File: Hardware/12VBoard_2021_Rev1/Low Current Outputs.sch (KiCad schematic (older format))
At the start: 54 parts

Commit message: Changed things
Dans a quitter
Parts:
- removed C?: 1000 uF, symbol Device:CP1
- removed C?: 100uF, symbol Device:C_Small
- removed Conn? (x2): AndersonPP, symbol MRDT_Connectors:AndersonPP
- removed D?: D_Schottky, symbol Device:D_Schottky
- removed D?: LED, symbol Device:LED
- removed L?: 100 uH, Inductor_SMD:L_0603_1608Metric_Pad1.05x0.95mm_HandSolder, symbol Device:L
- removed R?: 25m, symbol Device:R
- removed R?: 1.2k, symbol Device:R
- removed SW?: SW_SPDT, symbol Switch:SW_SPDT
- removed TP? (x2): TestPoint, symbol Connector:TestPoint
- removed U?: LM2576D2TR4, MRDT_Devices:LM2576, symbol 12VBoard_2021_Rev1-rescue:LM2576D2TR4-MRDT_Devices
- removed U?: INA198, Package_TO_SOT_SMD:SOT-23-5, symbol Amplifier_Current:INA198
- added R?: 25m, symbol Device:R
- added TP? (x2): TestPoint, symbol Connector:TestPoint
- added U?: INA198, Package_TO_SOT_SMD:SOT-23-5, symbol Amplifier_Current:INA198
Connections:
- net 5V: now also U?.3 (V+)
- net CurrentSense: now also TP?.1, U?.1
- net ExtraToggle: now also U?.5 (ON/OFF), TP?.1
- net GND: now also U?.2 (GND)
- net PackVoltage: now also R?.2, U?.4 (+); no longer C?.1, C?.1, C?.1, C?.1, U?.1 (VIN), U?.1 (VIN), U?.1 (VIN), U?.1 (VIN)
- net at C?.1, L?.2, U?.4 (FEEDBACK): now also Conn?.2 (V+Log), Conn?.2 (V+Log), R?.1
- new net: C?.1, C?.1, C?.1, C?.1, R?.1, U?.1 (VIN), U?.1 (VIN), U?.1 (VIN), U?.1 (VIN), U?.5 (-)

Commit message: Changed buck names
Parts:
- U? (x4): value LM2576D2TR4 -> LM2576S-12/NOPB
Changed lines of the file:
@@
 AR Path="/5F74F223/5F850762" Ref="U?"  Part="1"
 F 0 "U?" H 3100 1700 50  0000 C CNN
-F 1 "LM2576D2TR4" H 3100 1609 50  0000 C CNN
+F 1 "LM2576S-12/NOPB" H 3100 1609 50  0000 C CNN
 F 2 "MRDT_Devices:LM2576" H 3100 1725 50  0001 C CNN
 F 3 "https://www.mouser.com/datasheet/2/308/LM2576_D-1810688.pdf" H 3100 1725 50  0001 C CNN
@@
 AR Path="/5F74F223/5F853A40" Ref="U?"  Part="1"
 F 0 "U?" H 3125 2975 50  0000 C CNN
-F 1 "LM2576D2TR4" H 3125 2884 50  0000 C CNN
+F 1 "LM2576S-12/NOPB" H 3125 2884 50  0000 C CNN
 F 2 "MRDT_Devices:LM2576" H 3125 3000 50  0001 C CNN
 F 3 "https://www.mouser.com/datasheet/2/308/LM2576_D-1810688.pdf" H 3125 3000 50  0001 C CNN
@@
 AR Path="/5F74F223/5F8580AC" Ref="U?"  Part="1"
 F 0 "U?" H 3150 4225 50  0000 C CNN
-F 1 "LM2576D2TR4" H 3150 4134 50  0000 C CNN
+F 1 "LM2576S-12/NOPB" H 3150 4134 50  0000 C CNN
 F 2 "MRDT_Devices:LM2576" H 3150 4250 50  0001 C CNN
 F 3 "https://www.mouser.com/datasheet/2/308/LM2576_D-1810688.pdf" H 3150 4250 50  0001 C CNN
@@
 AR Path="/5F74F223/5F86A2E0" Ref="U?"  Part="1"
 F 0 "U?" H 3250 7000 50  0000 C CNN
-F 1 "LM2576D2TR4" H 3250 6909 50  0000 C CNN
+F 1 "LM2576S-12/NOPB" H 3250 6909 50  0000 C CNN
 F 2 "MRDT_Devices:LM2576" H 3250 7025 50  0001 C CNN
 F 3 "https://www.mouser.com/datasheet/2/308/LM2576_D-1810688.pdf" H 3250 7025 50  0001 C CNN

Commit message: fixed some stuffs
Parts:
- C10, C3, C4, C5, C6, C7, C8, C9: renamed from C?; footprint (none) -> Capacitor_SMD:C_0603_1608Metric_Pad1.05x0.95mm_HandSolder
- Conn1: renamed from Conn?; footprint (none) -> MRDT_Connectors:Anderson_2_Horizontal_Stacked
- D10, D11, D4, D5, D6, D7, D8, D9: renamed from D?; footprint (none) -> Diode_SMD:D_0603_1608Metric_Pad1.05x0.95mm_HandSolder
- R3: renamed from R?; value 25m -> 500m
- R4, R5, R6, R7: renamed from R?; footprint (none) -> Resistor_SMD:R_0603_1608Metric_Pad1.05x0.95mm_HandSolder
- TP1, TP2, TP3, TP4: renamed from TP?; footprint (none) -> TestPoint:TestPoint_Pad_2.5x2.5mm
- gave numbers to parts that had none: 14
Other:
- moved on the sheet: C10, C6, Conn6B, Conn7A, Conn7B, Conn8A, D11, D7, L5, R7, TP3, U6

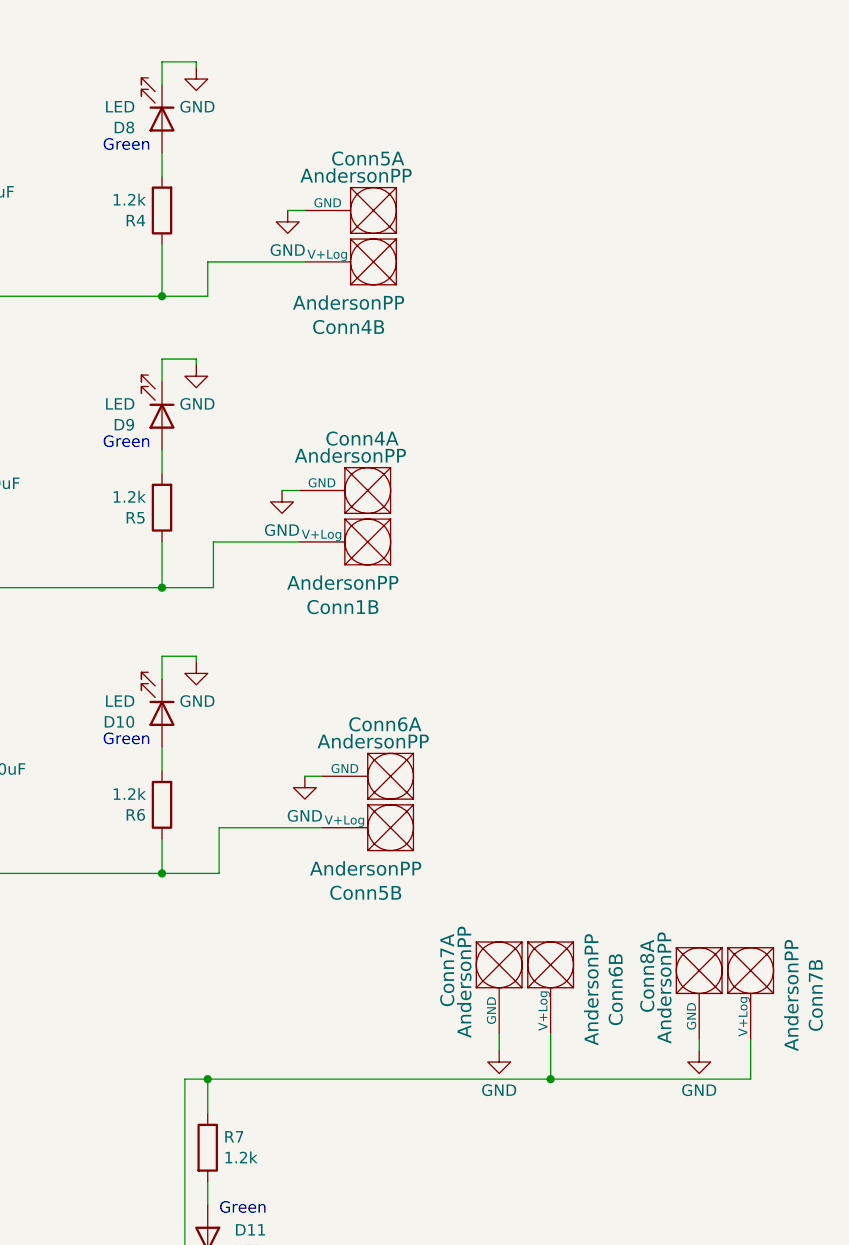
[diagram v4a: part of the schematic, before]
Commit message: Added Component Values.
Added values to high side buck and
 footprints to components.
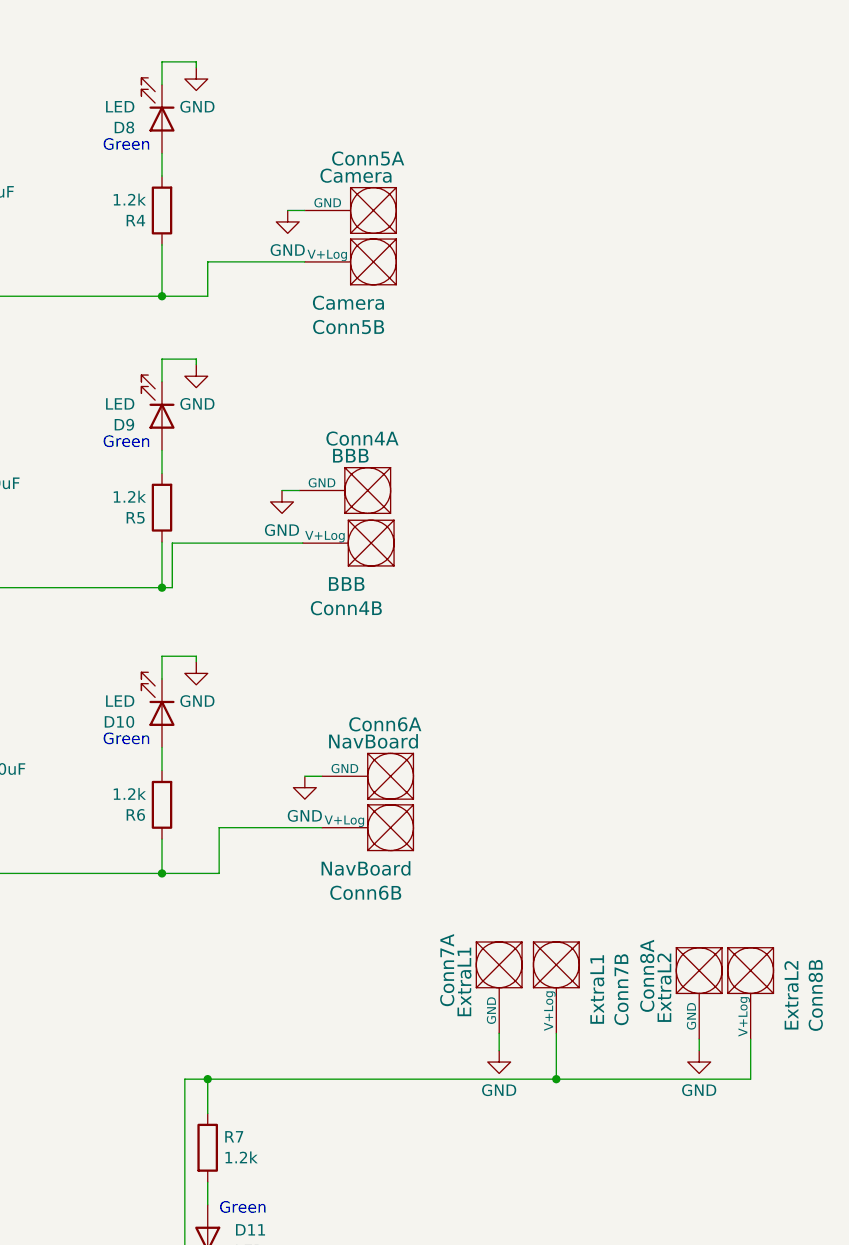
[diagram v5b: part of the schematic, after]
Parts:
- C3, C4, C5, C6: footprint Capacitor_SMD:C_0603_1608Metric_Pad1.05x0.95mm_HandSolder -> Capacitor_THT:CP_Axial_L20.0mm_D10.0mm_P26.00mm_Horizontal
- Conn4: value AndersonPP -> BBB; footprint (none) -> MRDT_Connectors:Anderson_2_Horizontal_Stacked
- Conn5: value AndersonPP -> Camera; footprint (none) -> MRDT_Connectors:Anderson_2_Horizontal_Stacked
- Conn6: value AndersonPP -> NavBoard; footprint (none) -> MRDT_Connectors:Anderson_2_Horizontal_Stacked
- Conn7: renamed from Conn1; value AndersonPP -> ExtraL1
- Conn7: value AndersonPP -> ExtraL1; footprint (none) -> MRDT_Connectors:Anderson_2_Horizontal_Stacked
- Conn8: renamed from Conn7; value AndersonPP -> ExtraL2; footprint (none) -> MRDT_Connectors:Anderson_2_Horizontal_Stacked
- Conn8: value AndersonPP -> ExtraL2; footprint (none) -> MRDT_Connectors:Anderson_2_Horizontal_Stacked
- R3: footprint (none) -> Resistor_SMD:R_1206_3216Metric_Pad1.30x1.75mm_HandSolder
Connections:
- net at C3.1, L2.2, R4.1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: now also Conn5.2 (V+Log); no longer Conn4.2 (V+Log)
- net at C4.1, L3.2, R5.1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: now also Conn4.2 (V+Log); no longer Conn7.2 (V+Log)
- net at C5.1, L4.2, R6.1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: now also Conn6.2 (V+Log); no longer Conn5.2 (V+Log)
- net at C6.1, Conn8.2 (V+Log), L5.2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: now also Conn7.2 (V+Log); no longer Conn6.2 (V+Log)
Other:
- moved on the sheet: Conn4B, Conn5B, Conn6B, Conn7B

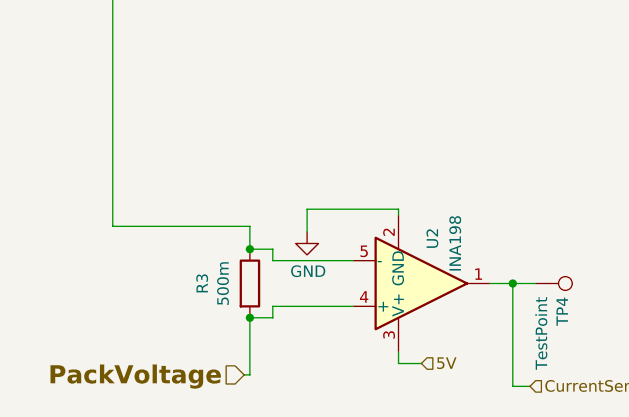
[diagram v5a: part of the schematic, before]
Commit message: Finished Footprint Assignment
added footprint for switch and finished footprint assigning aslwell as changeing low current current sense resistor to 50 m ohms.
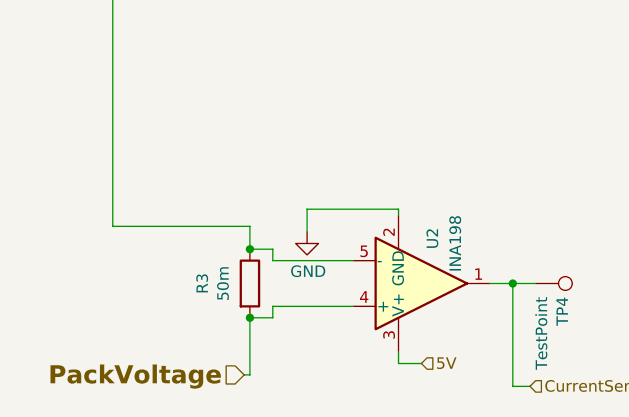
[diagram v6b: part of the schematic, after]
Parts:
- R3: value 500m -> 50m; footprint Resistor_SMD:R_1206_3216Metric_Pad1.30x1.75mm_HandSolder -> Resistor_SMD:R_2512_6332Metric_Pad1.52x3.35mm_HandSolder
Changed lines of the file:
@@
 AR Path="/5F74F223/5F8C9CDB" Ref="R3"  Part="1"
 F 0 "R3" V 1118 7275 50  0000 C CNN
-F 1 "500m" V 1209 7275 50  0000 C CNN
-F 2 "Resistor_SMD:R_1206_3216Metric_Pad1.30x1.75mm_HandSolder" V 1255 7275 50  0001 C CNN
+F 1 "50m" V 1209 7275 50  0000 C CNN
+F 2 "Resistor_SMD:R_2512_6332Metric_Pad1.52x3.35mm_HandSolder" V 1255 7275 50  0001 C CNN
 F 3 "~" H 1325 7275 50  0001 C CNN
 	1    1325 7275

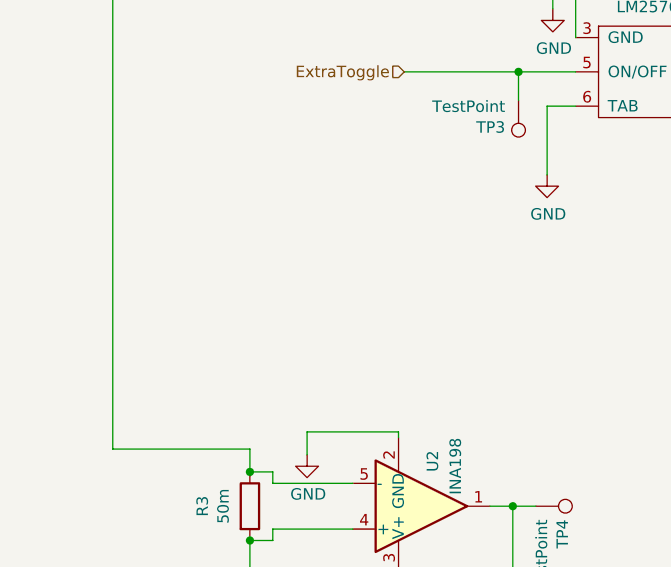
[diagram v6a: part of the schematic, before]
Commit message: Added Logic power circuits (High)
Added three smaller bucks for high current logic power and seprated acuation and logic pp
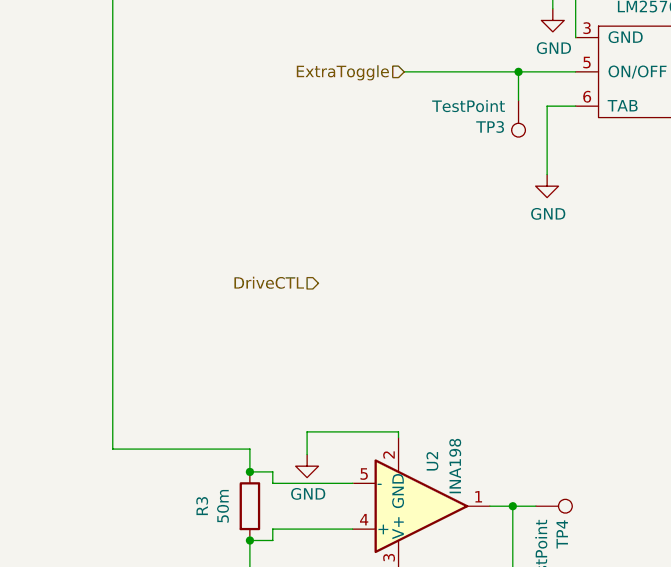
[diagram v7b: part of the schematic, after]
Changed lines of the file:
@@
 Wire Wire Line
 	6625 5275 8150 5275
+Text HLabel 1625 6300 0    50   Input ~ 0
+DriveCTL
 $EndSCHEMATC

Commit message: Layout Started
Board dimensions
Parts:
- added C43: 1000 uF, Capacitor_THT:CP_Axial_L20.0mm_D10.0mm_P26.00mm_Horizontal, symbol Device:CP1
- added C44: 100uF, Capacitor_SMD:C_0603_1608Metric_Pad1.05x0.95mm_HandSolder, symbol Device:C_Small
- added Conn15: Drive, MRDT_Connectors:Anderson_2_Horizontal_Stacked, symbol MRDT_Connectors:AndersonPP
- added D19: D_Schottky, Diode_SMD:D_0603_1608Metric_Pad1.05x0.95mm_HandSolder, symbol Device:D_Schottky
- added D20: LED, Diode_SMD:D_0603_1608Metric_Pad1.05x0.95mm_HandSolder, symbol Device:LED
- added L9: 100 uH, Inductor_SMD:L_0603_1608Metric_Pad1.05x0.95mm_HandSolder, symbol Device:L
- added R35: 1.2k, Resistor_SMD:R_0603_1608Metric_Pad1.05x0.95mm_HandSolder, symbol Device:R
- added TP8: TestPoint, TestPoint:TestPoint_Pad_2.5x2.5mm, symbol Connector:TestPoint
- added U14: LM2576S-12/NOPB, MRDT_Devices:LM2576, symbol 12VBoard_2021_Rev1-rescue:LM2576D2TR4-MRDT_Devices
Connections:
- net DriveCTL: now also TP8.1, U14.5 (ON/OFF)
- net GND: now also C43.2, C44.2, Conn15.1 (GND), D19.2 (A), D20.1 (K), U14.3 (GND), U14.6 (TAB)
- new net: D19.1 (K), L9.1, U14.2 (OUTPUT)
- new net: C43.1, Conn15.2 (V+Log), L9.2, R35.1, U14.4 (FEEDBACK)
- new net: C44.1, U14.1 (VIN)
- new net: D20.2 (A), R35.2
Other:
- moved on the sheet: C10, C6, Conn7A, Conn7B, Conn8A, Conn8B, D11, D7, L5, R7, TP3, U6
